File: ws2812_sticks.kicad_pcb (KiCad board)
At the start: 2 copper layers, 8.7 x 47.6 mm, 11 parts, among them J1 Conn_01x03_Socket, J2 Conn_01x03_Socket

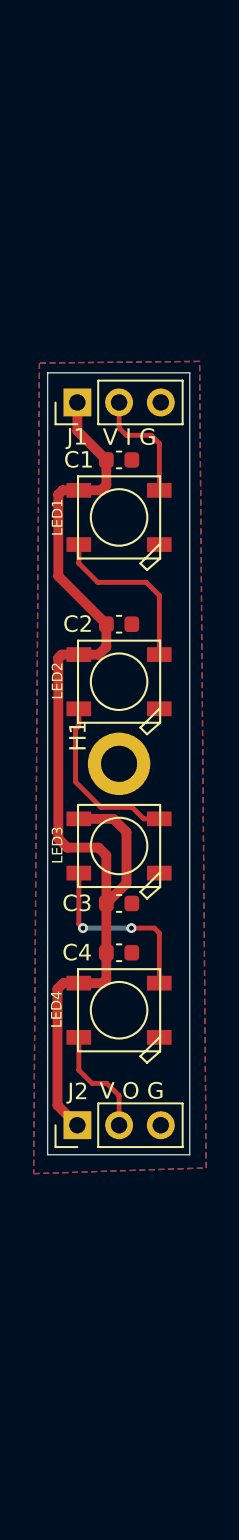
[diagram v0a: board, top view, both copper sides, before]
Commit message: created 8 led version
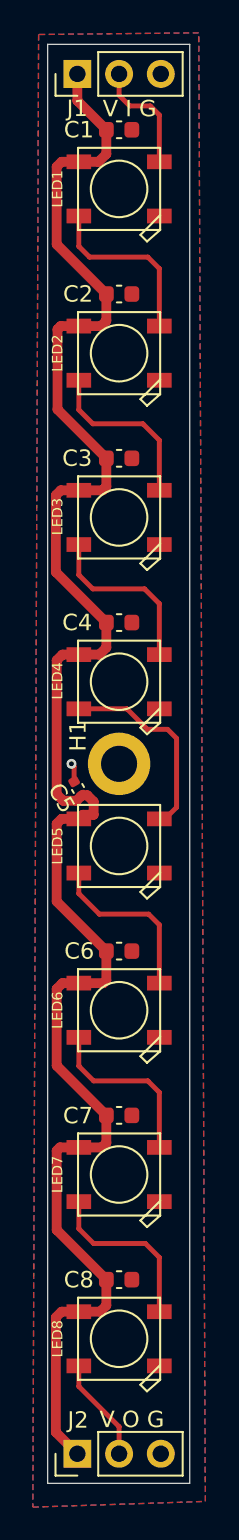
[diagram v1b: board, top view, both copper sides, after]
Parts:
- added C5: 100n, 0Capacitors:C_0402_1005Metric, F.Cu at (147.5, 101.5)
- added C6: 100n, 0Capacitors:C_0603_1608Metric, F.Cu at (150.0, 111.4)
- added C7: 100n, 0Capacitors:C_0603_1608Metric, F.Cu at (150.0, 121.4)
- added C8: 100n, 0Capacitors:C_0603_1608Metric, F.Cu at (150.0, 131.4)
- added LED5: WS2812, 0LED:WS2812B_5050, F.Cu at (150.0, 105.0)
- added LED6: WS2812, 0LED:WS2812B_5050, F.Cu at (150.0, 115.0)
- added LED7: WS2812, 0LED:WS2812B_5050, F.Cu at (150.0, 125.0)
- added LED8: WS2812, 0LED:WS2812B_5050, F.Cu at (150.0, 135.0)
- moved C3 27.1 mm to (150.0, 81.4)
- moved C1 20.1 mm to (150.0, 61.4)
- moved C2 20.1 mm to (150.0, 71.4)
- moved C4 20.1 mm to (150.0, 91.4)
- moved J1 20.0 mm to (147.5, 58.0)
- moved J2 20.0 mm to (147.5, 142.0)
- moved LED1 20.0 mm to (150.0, 65.0)
- moved LED2 20.0 mm to (150.0, 75.0)
- moved LED3 20.0 mm to (150.0, 85.0)
- moved LED4 20.0 mm to (150.0, 95.0)
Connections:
- LED4 pad 2-DOUT: /DOUT -> Net-(LED4-DO)
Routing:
- net VCC: track 64.6 -> 115.7 mm
- net Net-(LED4-DO): track 0.00 -> 12.2 mm
- net Net-(LED6-DO): track 0.00 -> 10.7 mm
- net Net-(LED7-DO): track 0.00 -> 10.6 mm
- net Net-(LED5-DO): track 0.00 -> 10.5 mm
- net GND: track 0.00 -> 1.15 mm, vias 0 -> 1
- net Net-(LED3-DO): track 11.3 -> 10.6 mm, vias 2 -> 0
- net /DOUT: track 6.89 -> 6.36 mm
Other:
- board size 8.7 x 47.6 mm -> 8.7 x 87.6 mm
